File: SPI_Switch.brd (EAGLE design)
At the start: 100 x 80 mm, 40 parts, among them J1 8516-4500PL, J2 1-406525-1, J3 1-406525-1, J4 0705510037, J5 0705510037, U1 TLE7230G, U2 SN74ABT126

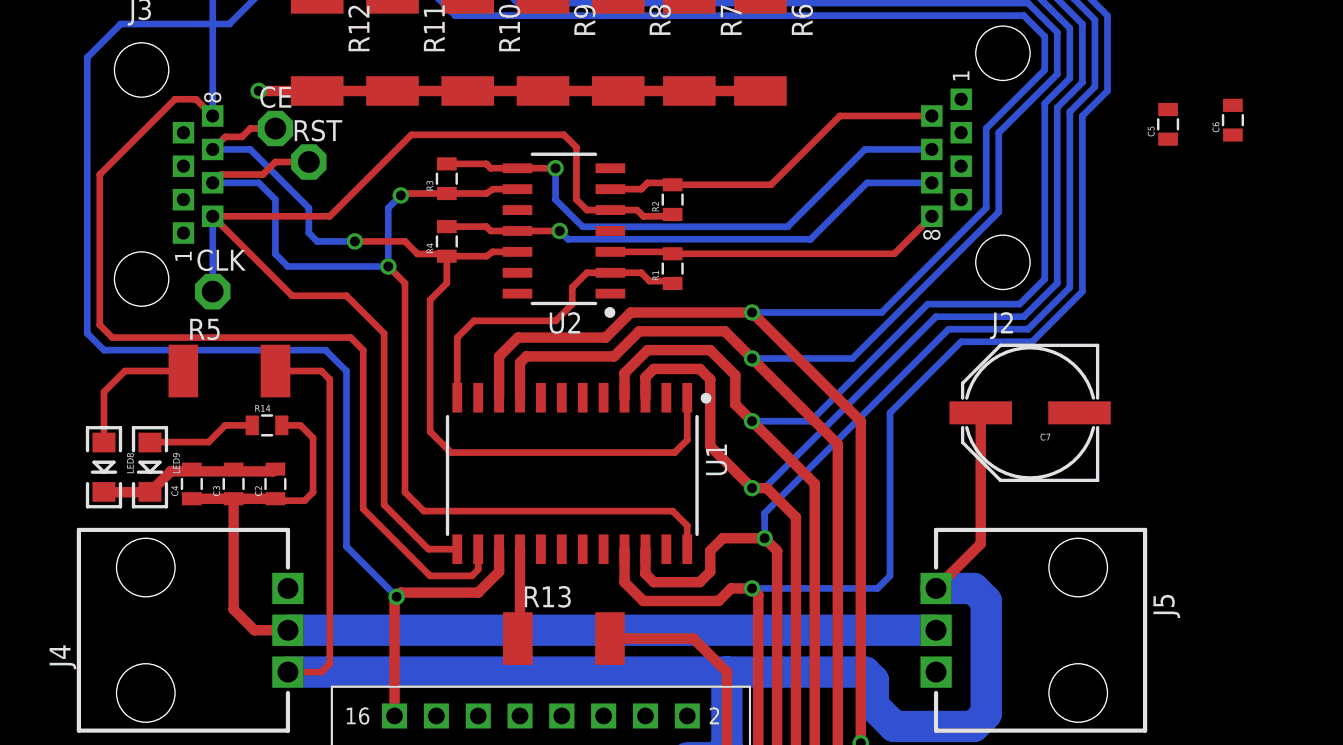
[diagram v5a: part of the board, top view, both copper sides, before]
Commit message: Finished routing except ground plane
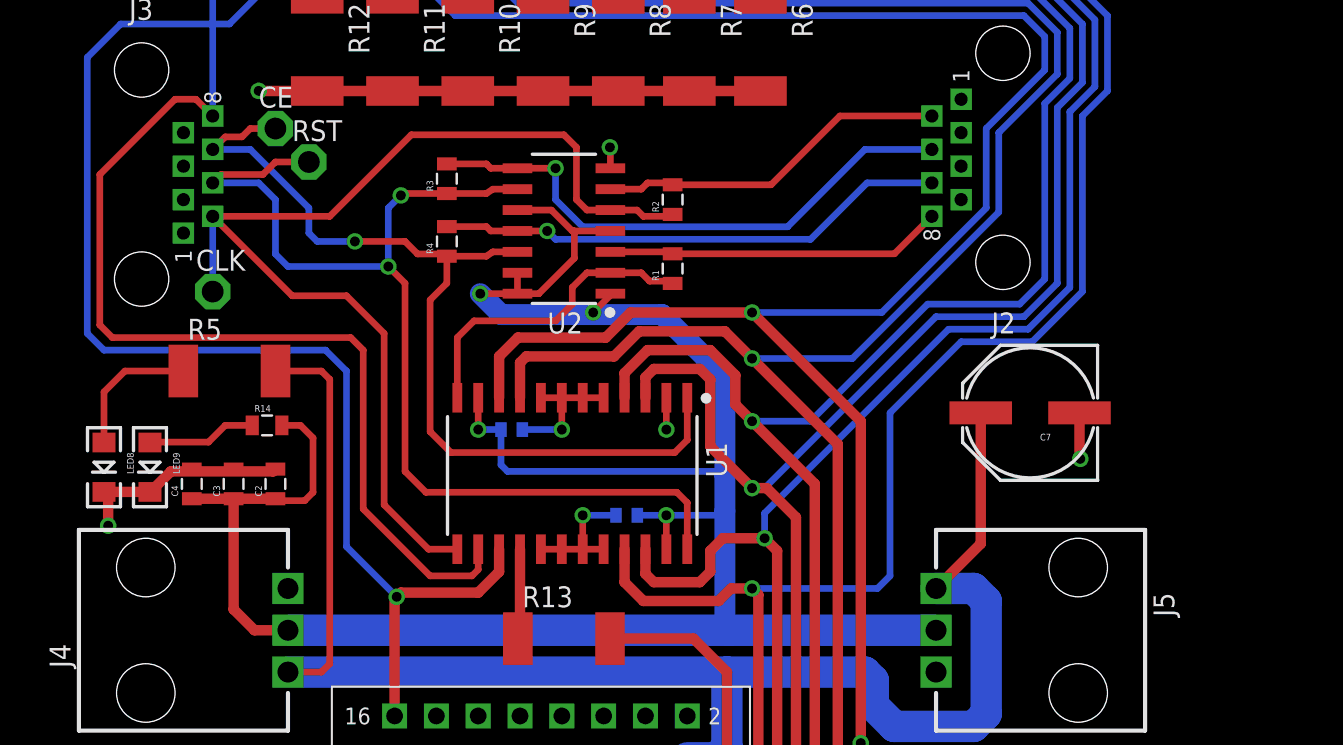
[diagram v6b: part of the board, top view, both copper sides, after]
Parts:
- removed C6: 10uF, SparkFun-Passives:0805
- added C1: (no value), SparkFun-Passives:0402-CAP
- C5: value 10uF -> (none); device SparkFun-Passives:0805 -> SparkFun-Passives:0402-CAP
- moved C5 40.6 mm to (39.6, 30.6), flipped to the bottom, turned to 0 degrees
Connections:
- net +5V: now also C1.1; no longer C6.1
- net GND: now also C1.2; no longer C6.2
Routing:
- net +5V: track 63.1 -> 139.6 mm, vias 0 -> 4
- net GND: track 11.0 -> 35.4 mm, vias 0 -> 6

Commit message: debugging drc errors
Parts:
- moved J2 10.9 mm to (56.1, 45.7)
- moved J3 10.9 mm to (8.89, 37.6)
- moved LED1 10.9 mm to (43.9, 55.9)
- moved LED2 10.9 mm to (39.6, 55.9)
- moved LED3 10.9 mm to (35.3, 55.9)
- moved LED4 10.9 mm to (30.7, 55.9)
- moved LED5 10.9 mm to (26.2, 55.9)
- moved LED6 10.9 mm to (21.6, 55.9)
- moved LED7 10.9 mm to (17.0, 55.9)
- moved R1 10.9 mm to (38.6, 35.4)
- moved R10 10.9 mm to (26.2, 49.0)
- moved R11 10.9 mm to (21.6, 49.0)
- moved R12 10.9 mm to (17.0, 49.0)
- moved R3 10.9 mm to (24.9, 40.9)
- moved R6 10.9 mm to (43.9, 49.0)
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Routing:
- net +24V: track 143.5 -> 222.6 mm, vias 1 -> 0
- added copper zone on layer 1, net GND
- added copper zone on layer 16, net GND

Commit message: 4 airwires left
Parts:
- moved CE 1.27 mm to (14.5, 45.2)
- moved J2 1.27 mm to (56.1, 47.0)
- moved J3 1.27 mm to (8.89, 38.9)
- moved LED8 1.27 mm to (4.06, 24.6)
- moved LED9 1.27 mm to (6.86, 24.6)
- moved R1 1.27 mm to (38.6, 36.7)
- moved R10 1.27 mm to (26.2, 50.3)
- moved R11 1.27 mm to (21.6, 50.3)
- moved R12 1.27 mm to (17.0, 50.3)
- moved R3 1.27 mm to (24.9, 42.2)
- moved R6 1.27 mm to (43.9, 50.3)
- moved R7 1.27 mm to (39.6, 50.3)
- moved R8 1.27 mm to (35.3, 50.3)
- moved R9 1.27 mm to (30.7, 50.3)
- moved RST 1.27 mm to (16.5, 43.2)
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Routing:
- net GND: track 35.4 -> 27.3 mm, vias 6 -> 23
- net +5V: track 139.6 -> 135.1 mm
- net N$7: track 1.91 -> 4.03 mm
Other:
- board text added: "CH1"
- board text added: "CH7"
- board text added: "Dec '13"
- board text added: "PWR IN"
- board text added: "PWR OUT"
- board text added: "SPI Driver"
- board text added: "SPI IN"
- board text added: "SPI OUT"
- board text added: "rev1"
